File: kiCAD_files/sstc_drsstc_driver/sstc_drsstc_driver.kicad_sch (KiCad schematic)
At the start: 80 parts, among them J1 Conn_01x02, J10 Conn_01x02, J11 Conn_01x03, J12 24V, J13 12V, J14 12V, J15 Conn_01x05, J16 Conn_01x05, J2 GDT, J3 Int_esp, J4 24V, J5 DRSSTC, J6 Conn_01x02, J7 SSTC, J8 DRSSTC, J9 SSTC_DUMMY, Q1 2N3904, U1 UCC27321P, U2 74HC14, U3 UCC27322P, U4 4N35, U5 ESP32-DEVKIT-V1, U7 74HC74, U8 LM7812_TO220, U9 LM7805_TO220

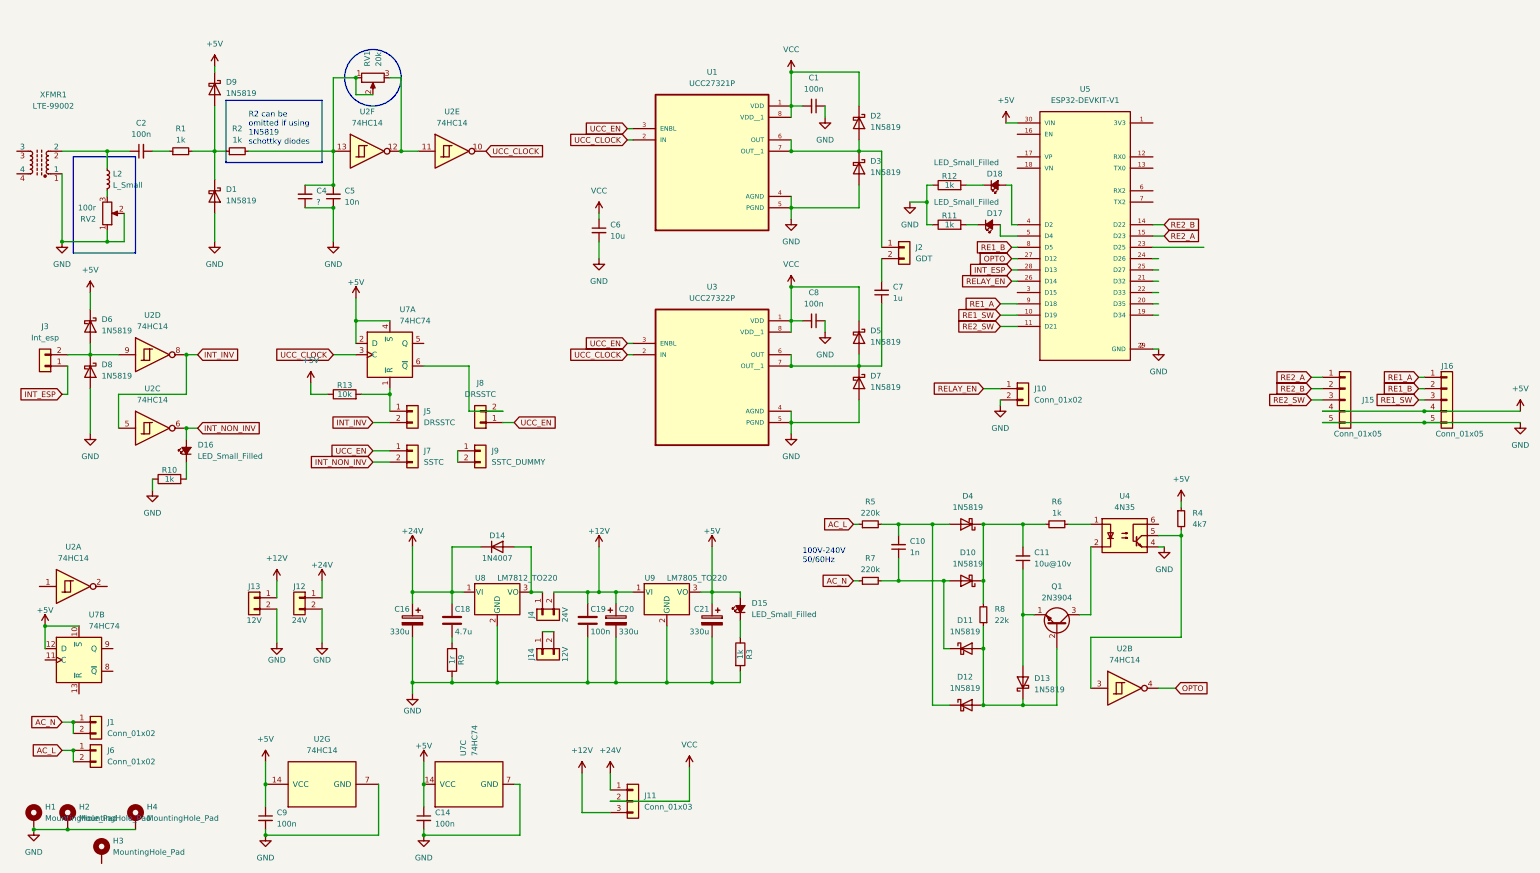
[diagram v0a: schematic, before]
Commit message: Add files via upload
Rotary encoders are now connected to 3.3V instead of 5V
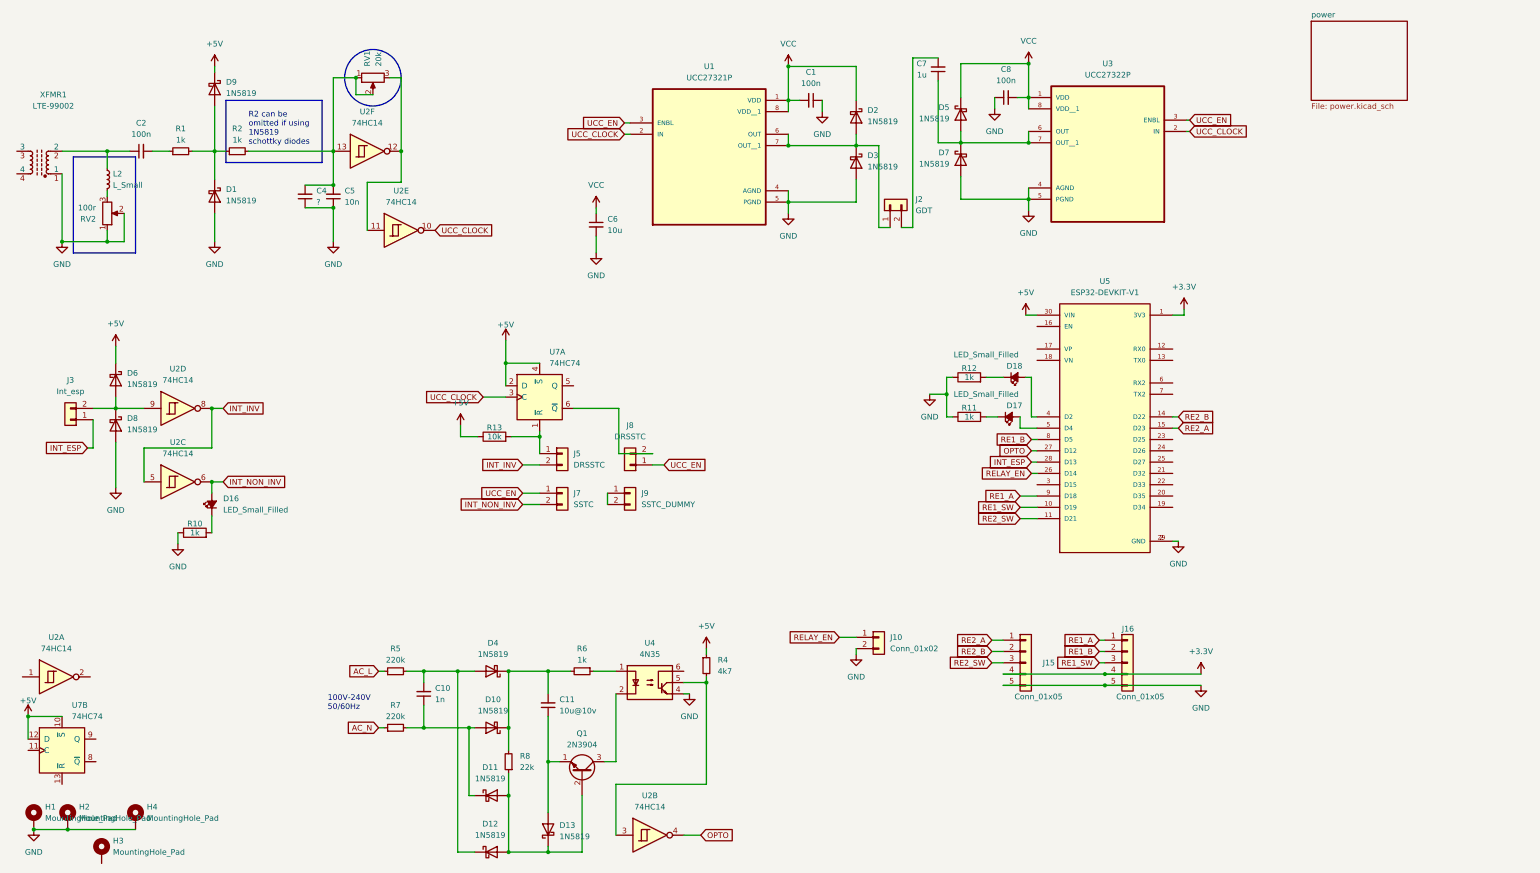
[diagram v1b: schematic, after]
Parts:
- removed C14, C9: 100n, Capacitor_SMD:C_1206_3216Metric, symbol Device:C_Small
- removed C16, C20, C21: 330u, Capacitor_THT:CP_Radial_D10.0mm_P5.00mm, symbol Device:C_Polarized
- removed C18: 4.7u, Capacitor_SMD:C_1206_3216Metric_Pad1.33x1.80mm_HandSolder, symbol Device:C
- removed C19: 100n, Capacitor_SMD:C_1206_3216Metric_Pad1.33x1.80mm_HandSolder, symbol Device:C
- removed D14: 1N4007, Diode_SMD:D_SOD-123, symbol Device:D
- removed D15: LED_Small_Filled, LED_THT:LED_D5.0mm_Clear, symbol Device:LED_Small_Filled
- removed J1, J6: Conn_01x02, Connector_PinSocket_2.54mm:PinSocket_1x02_P2.54mm_Vertical, symbol Connector_Generic:Conn_01x02
- removed J11: Conn_01x03, Connector_PinHeader_2.54mm:PinHeader_1x03_P2.54mm_Vertical, symbol Connector_Generic:Conn_01x03
- removed J12: 24V, TerminalBlock:TerminalBlock_bornier-2_P5.08mm, symbol Connector_Generic:Conn_01x02
- removed J13: 12V, TerminalBlock:TerminalBlock_bornier-2_P5.08mm, symbol Connector_Generic:Conn_01x02
- removed J14: 12V, Connector_PinHeader_2.54mm:PinHeader_1x02_P2.54mm_Vertical, symbol Connector_Generic:Conn_01x02
- removed J4: 24V, Connector_PinHeader_2.54mm:PinHeader_1x02_P2.54mm_Vertical, symbol Connector_Generic:Conn_01x02
- removed R3: 1k, Resistor_SMD:R_1206_3216Metric_Pad1.30x1.75mm_HandSolder, symbol Device:R
- removed R9: 1r, Resistor_SMD:R_1206_3216Metric_Pad1.30x1.75mm_HandSolder, symbol Device:R
- removed unit 7 of U2
- removed unit 3 of U7
- removed U8: LM7812_TO220, Package_TO_SOT_THT:TO-220-3_Vertical, symbol Regulator_Linear:LM7812_TO220
- removed U9: LM7805_TO220, Package_TO_SOT_THT:TO-220-3_Vertical, symbol Regulator_Linear:LM7805_TO220
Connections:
- net +5V: no longer J15.4 (Pin_4), J16.4 (Pin_4)
- net +3.3V: now reaches U5.1 (3V3)
- net +3.3V: now also J15.4 (Pin_4), J16.4 (Pin_4)
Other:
- added sheet power (power.kicad_sch)
- moved on the sheet: C1, C10, C11, C6, C7, C8, D10, D11, D12, D13, D16, D17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
